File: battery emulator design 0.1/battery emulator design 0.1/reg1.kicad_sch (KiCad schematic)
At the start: 7 parts, among them U1 LM324, U2 LM317_TO-220

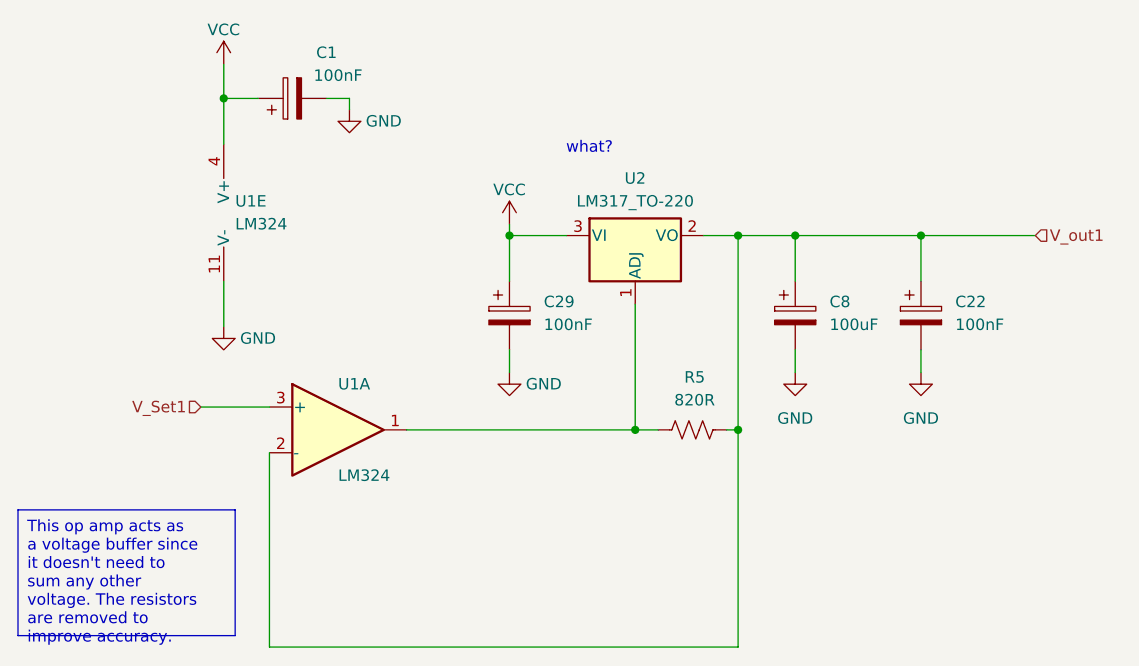
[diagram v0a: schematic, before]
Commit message: added pots to voltage buffers, other minor changes
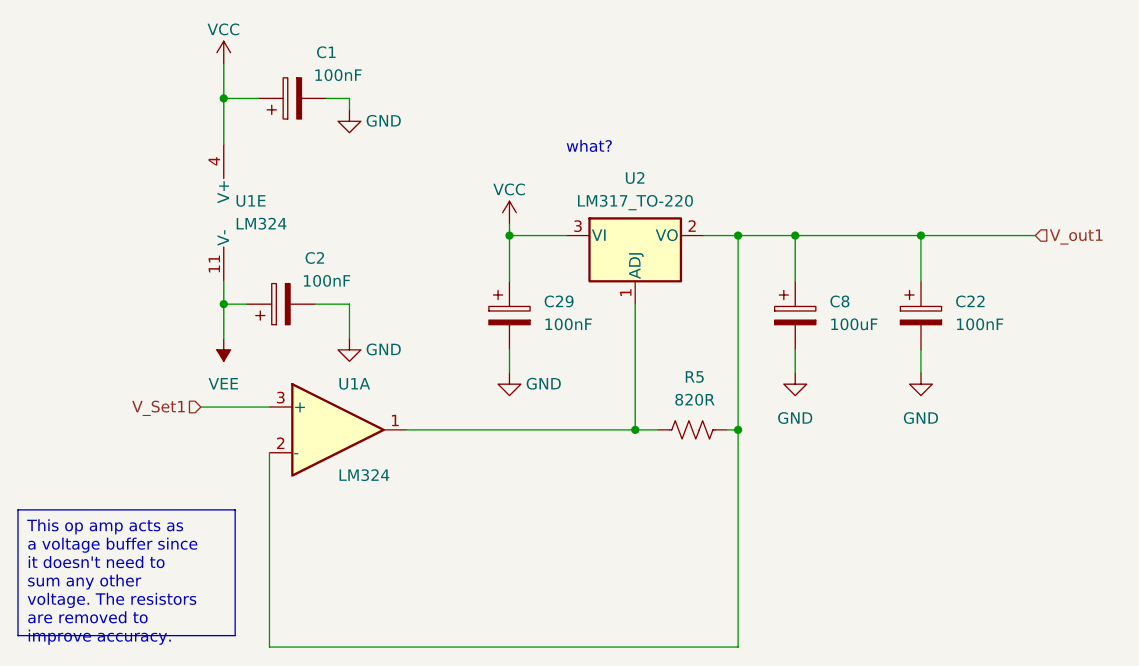
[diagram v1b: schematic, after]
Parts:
- added C2: 100nF, Capacitor_THT:C_Disc_D3.4mm_W2.1mm_P2.50mm, symbol Device:C_Polarized
- U1: footprint (none) -> Package_DIP:DIP-8_W7.62mm_LongPads
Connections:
- net GND: now also C2.2; no longer U1.11 (V-)
- new net VEE: C2.1, U1.11 (V-)
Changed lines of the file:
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@@
 		(color 0 0 0 0)
 	)
+	(junction
+		(at 124.46 86.36)
+		(diameter 0)
+		(color 0 0 0 0)
+	)
+	(wire
+		(pts
+			(xy 124.46 86.36) (xy 124.46 90.17)
+		)
+		(stroke
+			(width 0)
+			(type default)
+		)
+	)
 	(wire
 		(pts
@@
 	(wire
 		(pts
+			(xy 124.46 83.82) (xy 124.46 86.36)
+		)
+		(stroke
+			(width 0)
+			(type default)
+		)
+	)
+	(wire
+		(pts
 			(xy 162.56 78.74) (xy 156.21 78.74)
 		)
@@
 	(wire
 		(pts
+			(xy 124.46 86.36) (xy 127 86.36)
+		)
+		(stroke
+			(width 0)
+			(type default)
+		)
+	)
+	(wire
+		(pts
 			(xy 187.96 91.44) (xy 187.96 93.98)
 		)
@@
 	(wire
 		(pts
+			(xy 134.62 86.36) (xy 138.43 86.36)
+		)
+		(stroke
+			(width 0)
+			(type default)
+		)
+	)
+	(wire
+		(pts
 			(xy 135.89 63.5) (xy 138.43 63.5)
 		)
@@
 	(wire
 		(pts
-			(xy 124.46 83.82) (xy 124.46 88.9)
+			(xy 138.43 86.36) (xy 138.43 90.17)
 		)
 		(stroke
@@
 	)
 	(symbol
+		(lib_id "Device:C_Polarized")
+		(at 130.81 86.36 90)
+		(unit 1)
+		(exclude_from_sim no)
+		(in_bom yes)
+		(on_board yes)
+		(dnp no)
+		(property "Reference" "C2"
+			(at 134.62 81.28 90)
+			(effects
+				(font
+					(size 1.27 1.27)
+				)
+			)
+		)
+		(property "Value" "100nF"
+			(at 135.89 83.82 90)
+			(effects
+				(font
+					(size 1.27 1.27)
+				)
+			)
+		)
+		(property "Footprint" "Capacitor_THT:C_Disc_D3.4mm_W2.1mm_P2.50mm"
+			(at 134.62 85.3948 0)
+			(effects
+				(font
+					(size 1.27 1.27)
+				)
+				(hide yes)
+			)
+		)
+		(property "Datasheet" "~"
+			(at 130.81 86.36 0)
+			(effects
+				(font
+					(size 1.27 1.27)
+				)
+				(hide yes)
+			)
+		)
+		(property "Description" ""
+			(at 130.81 86.36 0)
+			(effects
+				(font
+					(size 1.27 1.27)
+				)
+				(hide yes)
+			)
+		)
+		(pin "1"
+		)
+		(pin "2"
+		)
+		(instances
+			(project "battery emulator design 0.1"
+				(path "/eb54f7d9-731a-4a54-adbe-3a25c9be0c1a/d3face5c-f429-4a6c-be18-8ab84a7159a2"
+					(reference "C2")
+					(unit 1)
+				)
+			)
+		)
+	)
+	(symbol
 		(lib_id "power:VCC")
 		(at 124.46 59.69 0)
@@
 			)
 		)
-		(property "Footprint" ""
+		(property "Footprint" "Package_DIP:DIP-8_W7.62mm_LongPads"
 			(at 125.73 73.66 0)
 			(effects
@@
 	)
 	(symbol
+		(lib_id "power:VEE")
+		(at 124.46 90.17 180)
+		(unit 1)
+		(exclude_from_sim no)
+		(in_bom yes)
+		(on_board yes)
+		(dnp no)
+		(fields_autoplaced yes)
+		(property "Reference" "#PWR01"
+			(at 124.46 86.36 0)
+			(effects
+				(font
+					(size 1.27 1.27)
+				)
+				(hide yes)
+			)
+		)
+		(property "Value" "VEE"
+			(at 124.46 95.25 0)
+			(effects
+				(font
+					(size 1.27 1.27)
+				)
+			)
+		)
+		(property "Footprint" ""
+			(at 124.46 90.17 0)
+			(effects
+				(font
+					(size 1.27 1.27)
+				)
+				(hide yes)
+			)
+		)
+		(property "Datasheet" ""
+			(at 124.46 90.17 0)
+			(effects
+				(font
+					(size 1.27 1.27)
+				)
+				(hide yes)
+			)
+		)
+		(property "Description" "Power symbol creates a global label with name \"VEE\""
+			(at 124.46 90.17 0)
+			(effects
+				(font
+					(size 1.27 1.27)
+				)
+				(hide yes)
+			)
+		)
+		(pin "1"
+		)
+		(instances
+			(project ""
+				(path "/eb54f7d9-731a-4a54-adbe-3a25c9be0c1a/d3face5c-f429-4a6c-be18-8ab84a7159a2"
+					(reference "#PWR01")
+					(unit 1)
+				)
+			)
+		)
+	)
+	(symbol
 		(lib_id "power:GND")
-		(at 124.46 88.9 0)
+		(at 138.43 90.17 0)
 		(unit 1)
 		(exclude_from_sim no)
@@
 		(dnp no)
 		(property "Reference" "#PWR045"
-			(at 124.46 95.25 0)
+			(at 138.43 96.52 0)
 			(effects
 				(font
@@
 		)
 		(property "Value" "GND"
-			(at 128.27 90.17 0)
+			(at 142.24 91.44 0)
 			(effects
 				(font
@@
 		)
 		(property "Footprint" ""
-			(at 124.46 88.9 0)
+			(at 138.43 90.17 0)
 			(effects
 				(font
@@
 		)
 		(property "Datasheet" ""
-			(at 124.46 88.9 0)
+			(at 138.43 90.17 0)
 			(effects
 				(font
@@
 		)
 		(property "Description" ""
-			(at 124.46 88.9 0)
-			(effects
-				(font
+			(at 138.43 90.17 0)
+			(effects
+				(font
